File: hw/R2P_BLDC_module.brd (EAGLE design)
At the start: 40 x 60 mm, 68 parts, among them Q1 OPTIMOS, Q2 OPTIMOS, Q3 OPTIMOS, Q4 OPTIMOS, Q5 OPTIMOS, Q6 OPTIMOS, U1 STM32F103CX, X1 MICROMATCH-4

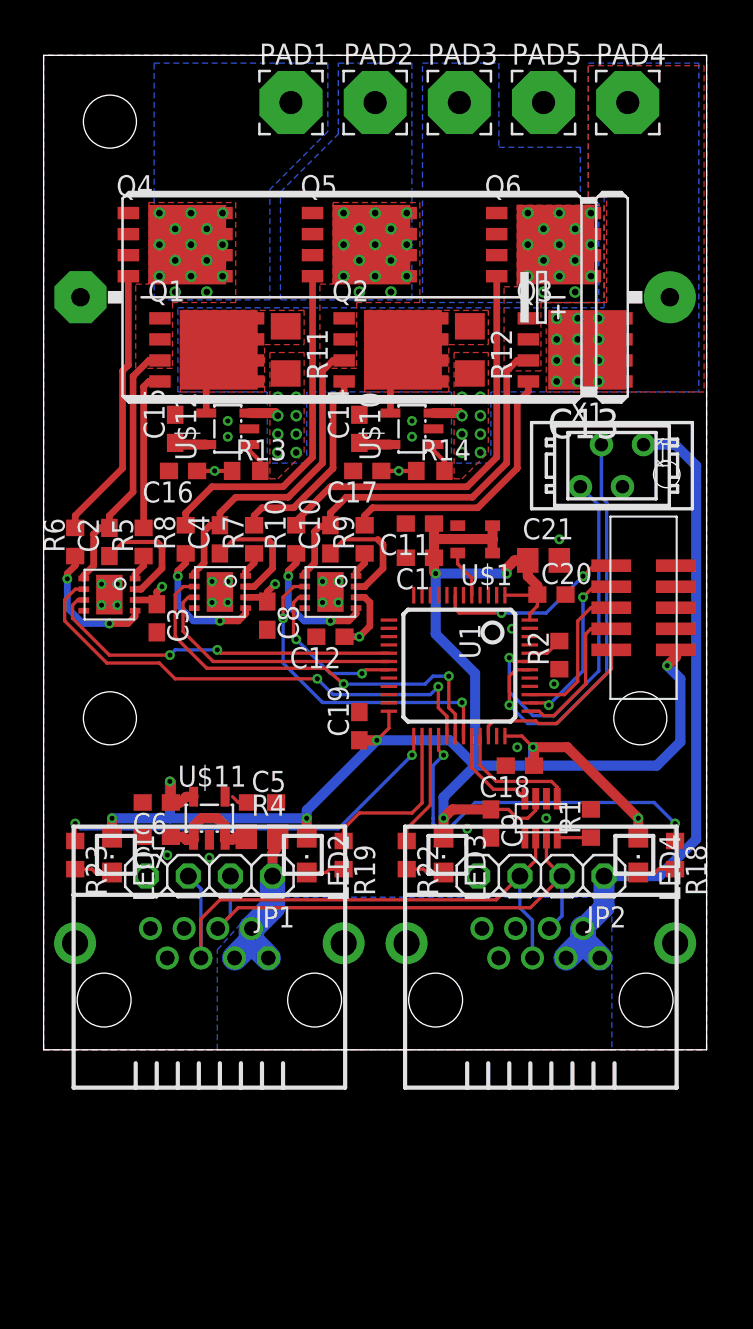
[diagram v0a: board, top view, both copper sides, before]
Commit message: hall connector to be placed
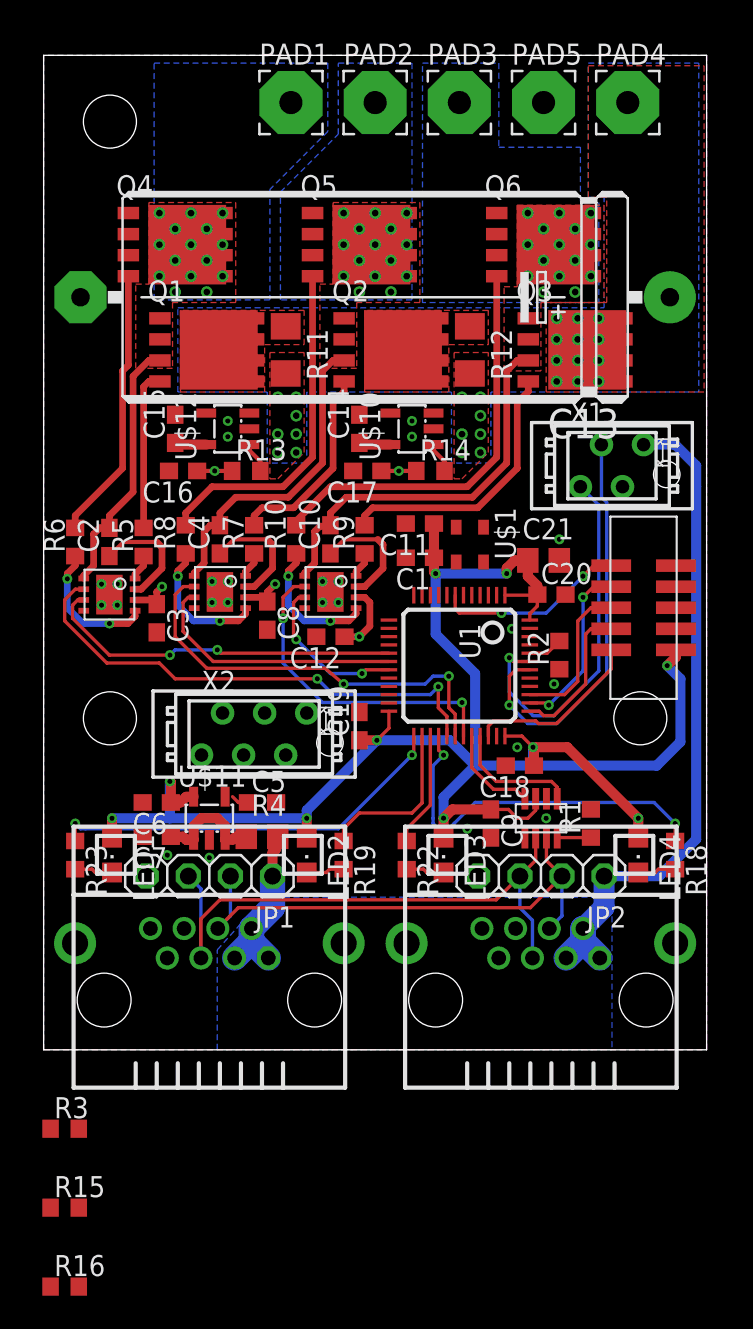
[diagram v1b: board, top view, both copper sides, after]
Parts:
- added R15, R16, R3: 4.7k, rcl:R0603
- added X2: MICROMATCH-6, apbteam_con-amp-micromatch:MICROMATCH-6
- moved U$1 0.45 mm to (25.7, 30.5), turned to 270 degrees
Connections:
- removed net N$14: Q1.5, Q1.6, Q1.7, Q1.8, Q1.TH, R11.1, U$12.4
- removed net N$16: Q2.5, Q2.6, Q2.7, Q2.8, Q2.TH, R12.1, U$10.4
- new net AI-: Q1.5, Q1.6, Q1.7, Q1.8, Q1.TH, R11.1
- new net HA: R3.1, X2.2
- new net HB: R15.1, X2.3
- new net HC: R16.1, X2.4
- new net IB-: Q2.5, Q2.6, Q2.7, Q2.8, Q2.TH, R12.1
- net +3V3: no longer U$1.1
- net +5V: now also R15.2, R16.2, R3.2, X2.1
- net +V: no longer U$10.3, U$12.3
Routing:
- net +3V3: track 113.1 -> 107.9 mm
- net +V: track 3.56 -> 0.00 mm, vias 28 -> 26
- net OSC_IN: track 2.90 -> 0.00 mm
- net N$16: track 1.99 -> 0.00 mm
- net N$14: track 1.60 -> 0.00 mm
- added copper zone on layer 1, net AI-
- added copper zone on layer 1, net IB-
- removed copper zone on layer 1, net N$14
- removed copper zone on layer 1, net N$16
